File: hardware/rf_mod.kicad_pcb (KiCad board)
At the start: 4 copper layers, 100 x 100 mm, 168 parts, among them J1001 SMA, J1002 SMA, J1003 SMA, J1004 Pmod, J101 SMA, J102 SMA, J103 SMA, J1201 SMA, J1202 SMA, J1301 SMA, J1302 SMA, J1303 SMA, J201 SMA, J202 SMA, J401 SMA, J402 SMA, J501 SMA, J502 SMA, J701 SMA, J702 SMA, J703 SMA, J801 SMA, J802 SMA, J803 SMA, J901 USB-C, J902 SMA, Q1001 AO3401A, Q1201 AO3401A, Q1301 AO3401A, Q501 AO3401A, Q701 AO3401A, Q801 AO3401A, SW1001 ON, SW1201 ON, SW1301 ON, SW501 ON, SW701 ON, SW801 ON, U1001 3.3V, U1002 MAX2871, U101 ADEX-10L+, U1201 GALI-84+, U1301 TRF3722, U1302 3.3V, U501 QPL9547, U701 3.3V, U702 ADL5350, U801 3.3V, U802 ADL5350, U901 MT3608, U902 3.3V, U903 74LVC1G17, X901 25 MHz

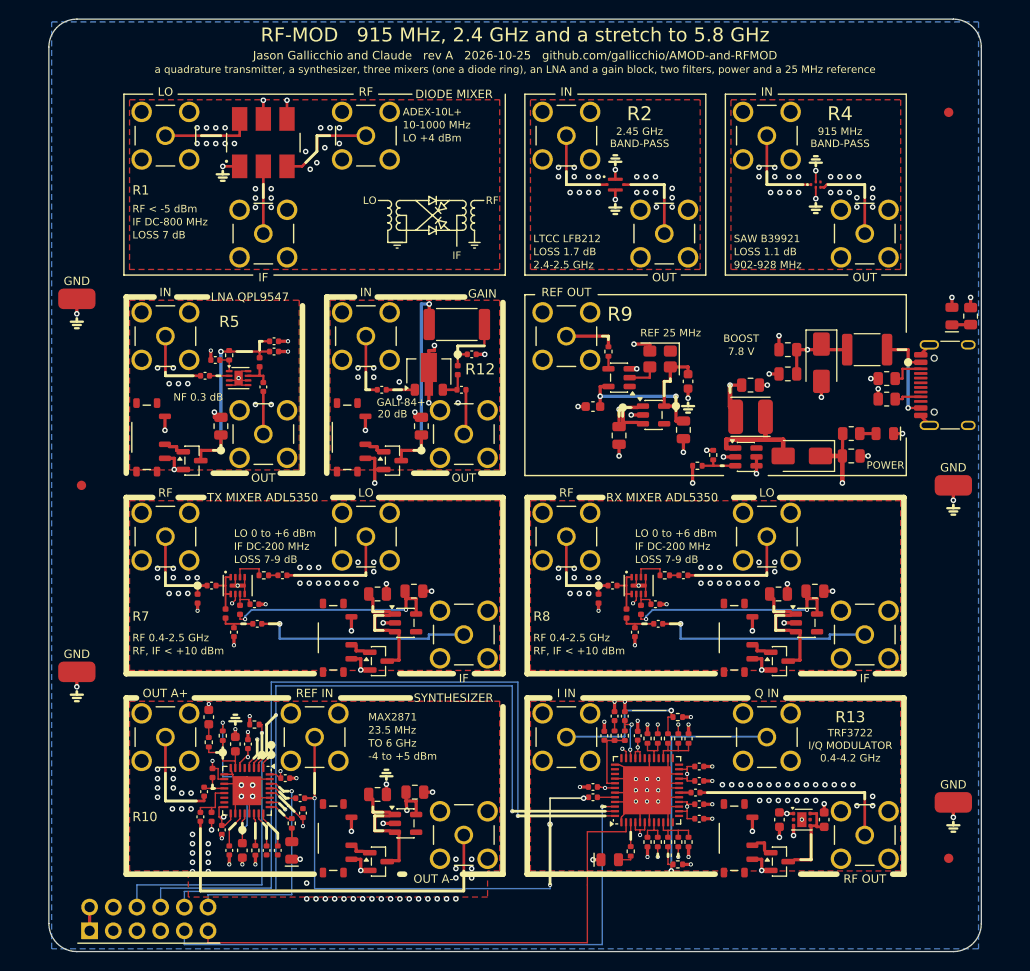
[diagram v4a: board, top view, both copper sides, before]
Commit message: Silk case convention on all six boards (Jason, Prompt 17: "To distinguish whole-tile labels from SMA or port labels, use different cases")
Ports (the jacks' names, terminal and loop names, a port named inside a note) stay UPPER CASE.  A tile's label (its
title on the frame, its name in the corner) is Mixed case: the first letter capitalised and the rest as written ("RC
low-pass", "Synthesizer", "I/Q demodulator"; tiles.label_case).  Ranges, values and notes are lower case except units,
acronyms and part numbers ("loss 1.7 dB", "OUT floats").  RF-MOD-2's X1 and X2 take word titles with their chips in
the info; RF-MOD's and RF-MOD-2's LNA tiles are titled "Preamp" ("Low-noise amp" does not fit a cell's frame); a few
two-line labels moved 0.15-0.3 mm for the descenders mixed case brings.  AMOD-P2's tile records (tile_docs), its DOA
list, KIT.md's AMOD-P2 section; X5's calibration points at P14.  All six boards: ERC 0, DRC 0, all fab checks.

Co-Authored-By: Claude Opus 5.5 <noreply@anthropic.com>
Claude-Session: https://claude.ai/code/session_01RKeoKvFFzjk3cEBLCXXHnB
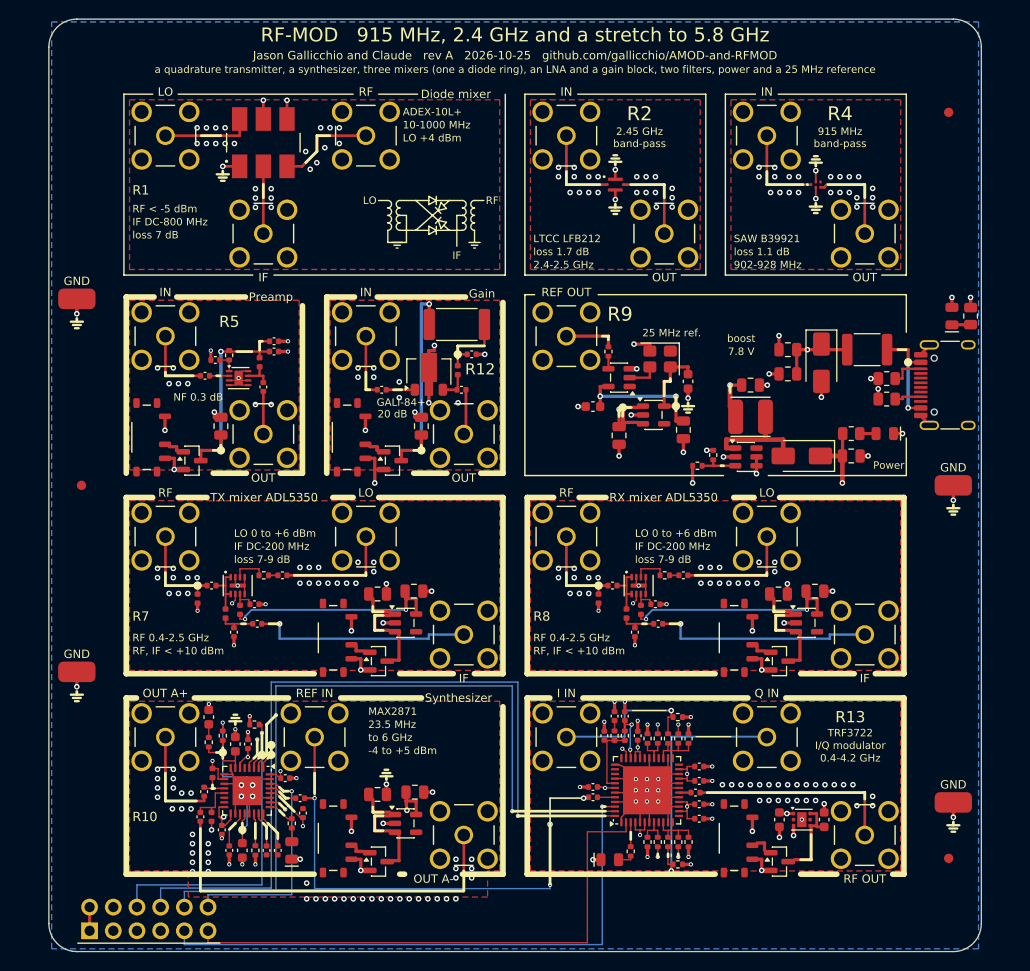
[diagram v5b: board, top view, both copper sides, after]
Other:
- board text added: "25 MHz ref."
- board text added: "Diode mixer"
- board text added: "Gain"
- board text added: "I/Q modulator"
- board text added: "Power"
- board text added: "Preamp"
- board text added: "RX mixer ADL5350"
- board text added: "Synthesizer"
- board text added: "TX mixer ADL5350"
- board text added: "band-pass"
- board text added: "boost"
- board text added: "loss 1.1 dB"
- board text added: "loss 1.7 dB"
- board text added: "loss 7 dB"
- board text added: "loss 7-9 dB"
- board text added: "to 6 GHz"
- board text removed: "BAND-PASS"
- board text removed: "BOOST"
- board text removed: "DIODE MIXER"
- board text removed: "GAIN"
- board text removed: "I/Q MODULATOR"
- board text removed: "LNA QPL9547"
- board text removed: "LOSS 1.1 dB"
- board text removed: "LOSS 1.7 dB"
- board text removed: "LOSS 7 dB"
- board text removed: "LOSS 7-9 dB"
- board text removed: "POWER"
- board text removed: "REF 25 MHz"
- board text removed: "RX MIXER ADL5350"
- board text removed: "SYNTHESIZER"
- board text removed: "TO 6 GHz"
- board text removed: "TX MIXER ADL5350"
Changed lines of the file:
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@@
 	(gr_line
 		(start 13.715714 29.8)
-		(end 17.011429 29.8)
+		(end 21.082856 29.8)
 		(stroke
 			(width 0.6)
@@
 	(gr_line
 		(start 13.865715 51.3)
-		(end 16.618572 51.3)
+		(end 16.961429 51.3)
 		(stroke
 			(width 0.6)
@@
 	(gr_line
 		(start 31.301429 72.8)
-		(end 38.768571 72.8)
+		(end 39.968571 72.8)
 		(stroke
 			(width 0.6)
@@
 	(gr_line
 		(start 35.215714 29.8)
-		(end 44.597143 29.8)
+		(end 44.682857 29.8)
 		(stroke
 			(width 0.6)
@@
 	(gr_line
 		(start 35.365715 8.05)
-		(end 38.940001 8.05)
+		(end 39.54 8.05)
 		(stroke
 			(width 0.15)
@@
 	(gr_line
 		(start 56.865715 51.3)
-		(end 59.404285 51.3)
+		(end 59.747142 51.3)
 		(stroke
 			(width 0.6)
@@
 		)
 	)
-	(gr_text "LOSS 7 dB"
+	(gr_text "loss 7 dB"
 		(at 8.95 23.15 0)
 		(layer "F.SilkS")
@@
 		)
 	)
-	(gr_text "LOSS 7-9 dB"
+	(gr_text "loss 7-9 dB"
 		(at 19.849999 57.949999 0)
 		(layer "F.SilkS")
@@
 	)
 	(gr_text "MAX2871"
-		(at 34.25 74.85 0)
+		(at 34.25 74.25 0)
 		(layer "F.SilkS")
 		(effects
@@
 	)
 	(gr_text "23.5 MHz"
-		(at 34.25 76.25 0)
+		(at 34.25 75.65 0)
 		(layer "F.SilkS")
 		(effects
@@
 		)
 	)
-	(gr_text "TO 6 GHz"
-		(at 34.25 77.649999 0)
+	(gr_text "to 6 GHz"
+		(at 34.25 77.05 0)
 		(layer "F.SilkS")
 		(effects
@@
 	)
 	(gr_text "-4 to +5 dBm"
-		(at 34.25 79.05 0)
+		(at 34.25 78.45 0)
 		(layer "F.SilkS")
 		(effects
@@
 		)
 	)
-	(gr_text "LOSS 1.7 dB"
+	(gr_text "loss 1.7 dB"
 		(at 51.95 24.95 0)
 		(layer "F.SilkS")
@@
 		)
 	)
-	(gr_text "LOSS 7-9 dB"
+	(gr_text "loss 7-9 dB"
 		(at 62.849999 57.949999 0)
 		(layer "F.SilkS")
@@
 		)
 	)
-	(gr_text "LOSS 1.1 dB"
+	(gr_text "loss 1.1 dB"
 		(at 73.45 24.95 0)
 		(layer "F.SilkS")
@@
 		)
 	)
-	(gr_text "BAND-PASS"
+	(gr_text "band-pass"
 		(at 63.35 13.35 0)
 		(layer "F.SilkS")
@@
 		)
 	)
-	(gr_text "BOOST"
+	(gr_text "boost"
 		(at 74.25 34.25 0)
 		(layer "F.SilkS")
@@
 		)
 	)
-	(gr_text "BAND-PASS"
+	(gr_text "band-pass"
 		(at 84.85 13.35 0)
 		(layer "F.SilkS")
@@
 		)
 	)
-	(gr_text "I/Q MODULATOR"
+	(gr_text "I/Q modulator"
 		(at 85.95 77.9 0)
 		(layer "F.SilkS")
@@
 		)
 	)
-	(gr_text "REF 25 MHz"
+	(gr_text "25 MHz ref."
 		(at 69.95 33.65 0)
 		(layer "F.SilkS")
@@
 		)
 	)
-	(gr_text "POWER"
+	(gr_text "Power"
 		(at 91.75 47.85 0)
 		(layer "F.SilkS")
@@
 		)
 	)
-	(gr_text "TX MIXER ADL5350"
-		(at 16.968572 51.3 0)
+	(gr_text "TX mixer ADL5350"
+		(at 17.311429 51.3 0)
 		(layer "F.SilkS")
 		(effects
@@
 		)
 	)
-	(gr_text "LNA QPL9547"
-		(at 17.361429 29.8 0)
+	(gr_text "Preamp"
+		(at 21.432856 29.8 0)
 		(layer "F.SilkS")
 		(effects
@@
 		)
 	)
-	(gr_text "SYNTHESIZER"
-		(at 39.118571 72.8 0)
+	(gr_text "Diode mixer"
+		(at 39.89 8.05 0)
 		(layer "F.SilkS")
 		(effects
@@
 		)
 	)
-	(gr_text "DIODE MIXER"
-		(at 39.290001 8.05 0)
+	(gr_text "Synthesizer"
+		(at 40.318571 72.8 0)
 		(layer "F.SilkS")
 		(effects
@@
 		)
 	)
-	(gr_text "GAIN"
-		(at 44.947143 29.45 0)
+	(gr_text "Gain"
+		(at 45.032857 29.45 0)
 		(layer "F.SilkS")
 		(effects
@@
 		)
 	)
-	(gr_text "RX MIXER ADL5350"
-		(at 59.754285 51.3 0)
+	(gr_text "RX mixer ADL5350"
+		(at 60.097142 51.3 0)
 		(layer "F.SilkS")
 		(effects
